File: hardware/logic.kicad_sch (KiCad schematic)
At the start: 64 parts, among them J1 Hanrun HY931147C, SW1 SW_Push, U2 KSZ8851SNL, U3 SRV05-4, U4 ESP32-C3-WROOM-02, U5 AMS1117-3.3, Y1 25MHz

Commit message: rev 0.4 move button next to ethernet jack, kicad v9
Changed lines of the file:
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@@
 (kicad_sch
-	(version 20231120)
+	(version 20250114)
 	(generator "eeschema")
-	(generator_version "8.0")
+	(generator_version "9.0")
 	(paper "A4")
+	(text "Alternate parts:\nHanRun HY931147C\nHCTL HC931147C\n"
+		(exclude_from_sim no)
+		(at 242.062 104.902 0)
+		(effects
+			(font
+				(size 1.27 1.27)
+			)
+			(justify left)
+		)
+	)
+	(text "TODO: evaluate if D5 drops voltage enough\nto not need voltage level translation on LEDs"
+		(exclude_from_sim no)
+		(at 39.624 17.78 0)
+		(effects
+			(font
+				(size 1.27 1.27)
+			)
+		)
+	)
 	(junction
 		(at 40.64 99.06)
@@
 		)
 	)
-	(text "Alternate parts:\nHanRun HY931147C\nHCTL HC931147C\n"
-		(exclude_from_sim no)
-		(at 242.062 104.902 0)
-		(effects
-			(font
-				(size 1.27 1.27)
-			)
-			(justify left)
-		)
-	)
-	(text "TODO: evaluate if D5 drops voltage enough\nto not need voltage level translation on LEDs"
-		(exclude_from_sim no)
-		(at 39.624 17.78 0)
-		(effects
-			(font
-				(size 1.27 1.27)
-			)
-		)
-	)
 	(label "D-"
 		(at 64.77 139.7 180)
@@
 		(at 34.29 29.21)
 		(size 15.24 17.78)
+		(exclude_from_sim no)
+		(in_bom yes)
+		(on_board yes)
+		(dnp no)
 		(fields_autoplaced yes)
 		(stroke

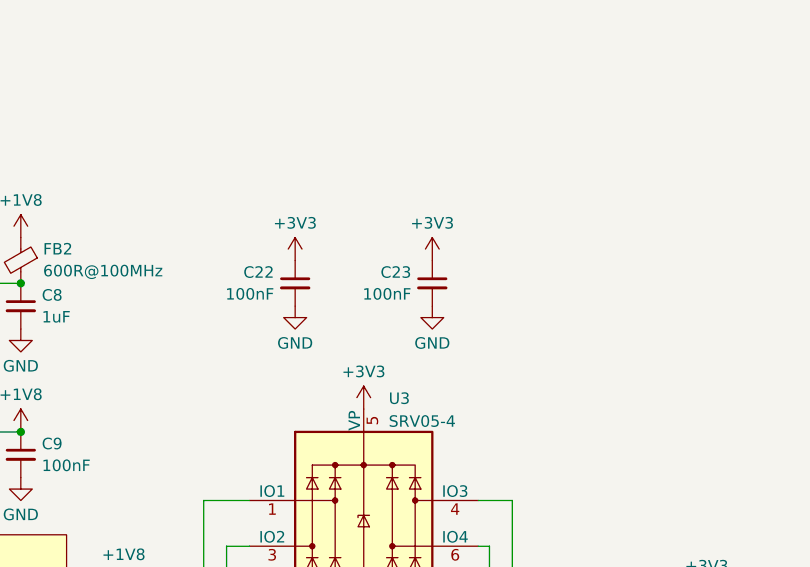
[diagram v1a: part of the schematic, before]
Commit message: Update button footprint library reference
The library symbol was previously changed in the PCB design file only.
Relfect that change in the schematic, too.
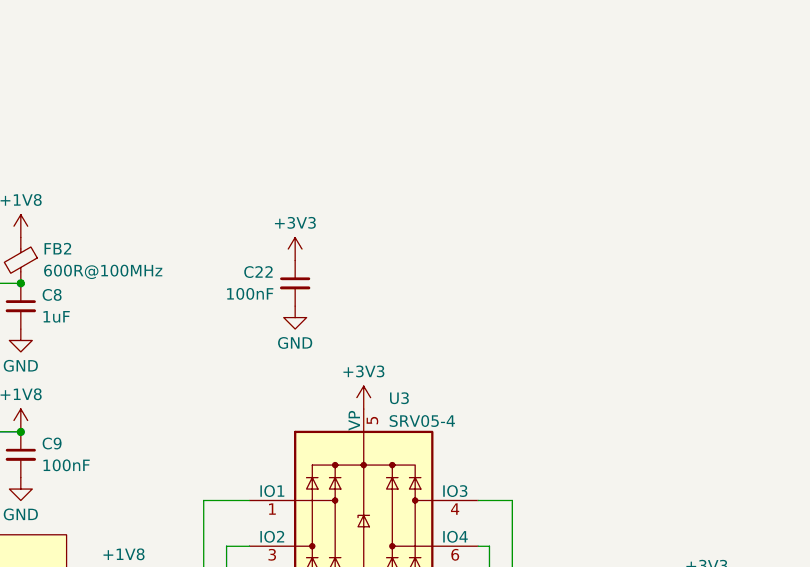
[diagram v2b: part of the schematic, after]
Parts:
- removed C23: 100nF, Capacitor_SMD:C_0402_1005Metric, symbol Device:C_Small
- SW1: footprint Button_Switch_SMD_LCSC:x-1825027-x -> Button_Switch_SMD_LCSC_Shorter:KEY-TH_4P-L7.5-W6.8-P4.50-LS7.2
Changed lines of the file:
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@@
 	)
 	(symbol
-		(lib_id "Device:C_Small")
-		(at 193.04 68.58 0)
-		(unit 1)
-		(exclude_from_sim no)
-		(in_bom yes)
-		(on_board yes)
-		(dnp no)
-		(property "Reference" "C23"
-			(at 190.7159 67.3741 0)
-			(effects
-				(font
-					(size 1.27 1.27)
-				)
-				(justify right)
-			)
-		)
-		(property "Value" "100nF"
-			(at 190.7159 69.7984 0)
-			(effects
-				(font
-					(size 1.27 1.27)
-				)
-				(justify right)
-			)
-		)
-		(property "Footprint" "Capacitor_SMD:C_0402_1005Metric"
-			(at 193.04 68.58 0)
-			(effects
-				(font
-					(size 1.27 1.27)
-				)
-				(hide yes)
-			)
-		)
-		(property "Datasheet" "~"
-			(at 193.04 68.58 0)
-			(effects
-				(font
-					(size 1.27 1.27)
-				)
-				(hide yes)
-			)
-		)
-		(property "Description" "Unpolarized capacitor, small symbol"
-			(at 193.04 68.58 0)
-			(effects
-				(font
-					(size 1.27 1.27)
-				)
-				(hide yes)
-			)
-		)
-		(property "LCSC" "C1525"
-			(at 193.04 68.58 0)
-			(effects
-				(font
-					(size 1.27 1.27)
-				)
-				(hide yes)
-			)
-		)
-		(pin "2"
-		)
-		(pin "1"
-		)
-		(instances
-			(project "TallyLight"
-				(path "/d4f869dd-5485-4b4f-b239-21313c2a8e4c/7cb40ab1-1706-4709-9063-b880462d2aa7"
-					(reference "C23")
-					(unit 1)
-				)
-			)
-		)
-	)
-	(symbol
 		(lib_name "GND_7")
 		(lib_id "power:GND")
@@
 	)
 	(symbol
-		(lib_name "GND_7")
-		(lib_id "power:GND")
-		(at 193.04 71.12 0)
-		(unit 1)
-		(exclude_from_sim no)
-		(in_bom yes)
-		(on_board yes)
-		(dnp no)
-		(fields_autoplaced yes)
-		(property "Reference" "#PWR49"
-			(at 193.04 77.47 0)
-			(effects
-				(font
-					(size 1.27 1.27)
-				)
-				(hide yes)
-			)
-		)
-		(property "Value" "GND"
-			(at 193.04 75.2531 0)
-			(effects
-				(font
-					(size 1.27 1.27)
-				)
-			)
-		)
-		(property "Footprint" ""
-			(at 193.04 71.12 0)
-			(effects
-				(font
-					(size 1.27 1.27)
-				)
-				(hide yes)
-			)
-		)
-		(property "Datasheet" ""
-			(at 193.04 71.12 0)
-			(effects
-				(font
-					(size 1.27 1.27)
-				)
-				(hide yes)
-			)
-		)
-		(property "Description" "Power symbol creates a global label with name \"GND\" , ground"
-			(at 193.04 71.12 0)
-			(effects
-				(font
-					(size 1.27 1.27)
-				)
-				(hide yes)
-			)
-		)
-		(pin "1"
-		)
-		(instances
-			(project "TallyLight"
-				(path "/d4f869dd-5485-4b4f-b239-21313c2a8e4c/7cb40ab1-1706-4709-9063-b880462d2aa7"
-					(reference "#PWR49")
-					(unit 1)
-				)
-			)
-		)
-	)
-	(symbol
 		(lib_name "GND_3")
 		(lib_id "power:GND")
@@
 			)
 		)
-		(property "Footprint" "Button_Switch_SMD_LCSC:x-1825027-x"
+		(property "Footprint" "Button_Switch_SMD_LCSC_Shorter:KEY-TH_4P-L7.5-W6.8-P4.50-LS7.2"
 			(at 66.04 173.99 0)
 			(effects
@@
 					(unit 1)
 				)
-			)
-		)
-	)
-	(symbol
-		(lib_name "+3V3_1")
-		(lib_id "power:+3V3")
-		(at 193.04 66.04 0)
-		(unit 1)
-		(exclude_from_sim no)
-		(in_bom yes)
-		(on_board yes)
-		(dnp no)
-		(fields_autoplaced yes)
-		(property "Reference" "#PWR50"
-			(at 193.04 69.85 0)
-			(effects
-				(font
-					(size 1.27 1.27)
-				)
-				(hide yes)
-			)
-		)
-		(property "Value" "+3V3"
-			(at 193.04 61.9069 0)
-			(effects
-				(font
-					(size 1.27 1.27)
-				)
-			)
-		)
-		(property "Footprint" ""
-			(at 193.04 66.04 0)
-			(effects
-				(font
-					(size 1.27 1.27)
-				)
-				(hide yes)
-			)
-		)
-		(property "Datasheet" ""
-			(at 193.04 66.04 0)
-			(effects
-				(font
-					(size 1.27 1.27)
-				)
-				(hide yes)
-			)
-		)
-		(property "Description" "Power symbol creates a global label with name \"+3V3\""
-			(at 193.04 66.04 0)
-			(effects
-				(font
-					(size 1.27 1.27)
-				)
-				(hide yes)
-			)
-		)
-		(pin "1"
-		)
-		(instances
-			(project "TallyLight"
-				(path "/d4f869dd-5485-4b4f-b239-21313c2a8e4c/7cb40ab1-1706-4709-9063-b880462d2aa7"
-					(reference "#PWR50")
-					(unit 1)
-				)
